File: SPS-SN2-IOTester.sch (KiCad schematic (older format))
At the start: 26 parts, among them J1 RJ45, J2 Spade Terminal, SW1 SW, SW2 SW, SW3 SW, SW4 SW, SW5 SW, SW6 SW, SW7 SW, SW8 SW

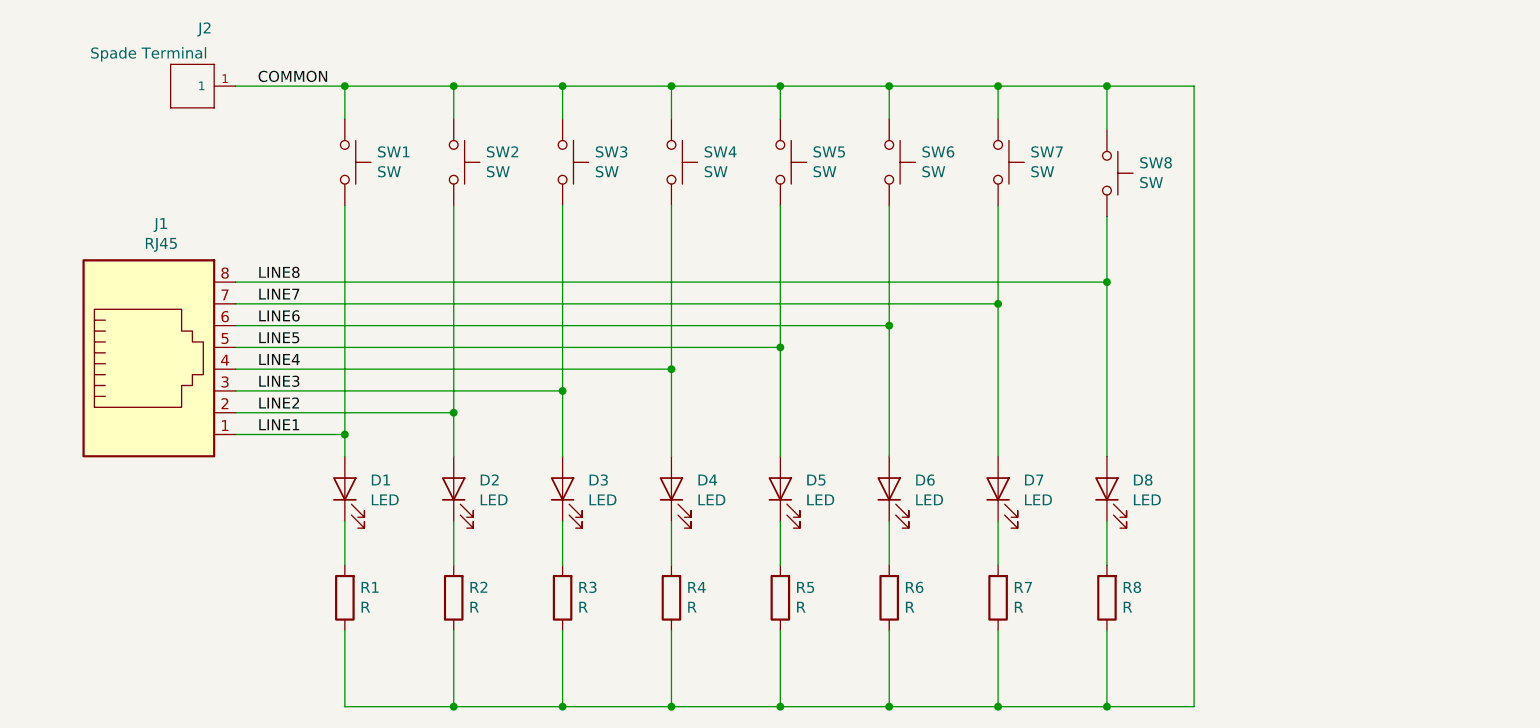
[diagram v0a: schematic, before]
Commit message: added schematic annotation
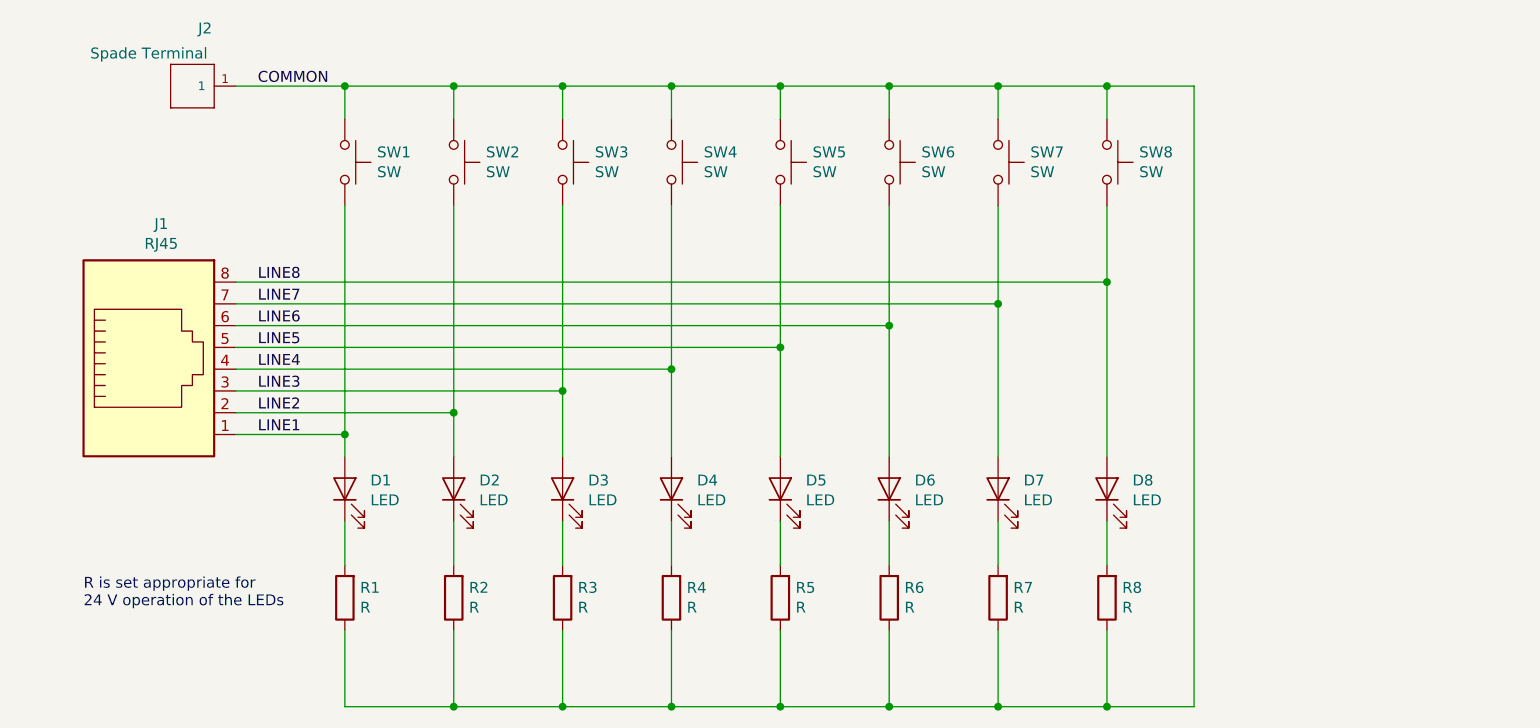
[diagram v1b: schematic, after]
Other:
- note added: "R is set appropriate for \n24 V operation of the LEDs"
- moved on the sheet: SW8
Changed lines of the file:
@@
 L Switch:SW_Push SW8
 U 1 1 5E0A6255
-P 7800 2600
-F 0 "SW8" V 7754 2748 50  0000 L CNN
-F 1 "SW" V 7845 2748 50  0000 L CNN
-F 2 "Button_Switch_THT:SW_PUSH_6mm_H5mm" H 7800 2800 50  0001 C CNN
-F 3 "~" H 7800 2800 50  0001 C CNN
-	1    7800 2600
+P 7800 2550
+F 0 "SW8" V 7754 2698 50  0000 L CNN
+F 1 "SW" V 7845 2698 50  0000 L CNN
+F 2 "Button_Switch_THT:SW_PUSH_6mm_H5mm" H 7800 2750 50  0001 C CNN
+F 3 "~" H 7800 2750 50  0001 C CNN
+	1    7800 2550
 	0    1    1    0
 $EndComp
-Wire Wire Line
-	7800 3100 7800 2800
 Connection ~ 7800 3100
 Wire Wire Line
@@
 	7300 2200 7300 2350
 Connection ~ 6800 2200
-Wire Wire Line
-	7300 2200 7800 2200
-Wire Wire Line
-	7800 2200 7800 2400
 Connection ~ 7300 2200
 Wire Wire Line
 	5800 5050 6300 5050
 Wire Wire Line
-	7800 2200 8200 2200
-Wire Wire Line
 	8200 2200 8200 5050
 Wire Wire Line
 	8200 5050 7800 5050
-Connection ~ 7800 2200
 Connection ~ 7800 5050
 $Comp
@@
 Text Label 3900 3100 0    50   ~ 0
 LINE8
+Wire Wire Line
+	7300 2200 7800 2200
+Wire Wire Line
+	7800 2350 7800 2200
+Connection ~ 7800 2200
+Wire Wire Line
+	7800 2200 8200 2200
+Wire Wire Line
+	7800 2750 7800 3100
+Text Notes 3100 4600 0    50   ~ 0
+R is set appropriate for \n24 V operation of the LEDs
 $EndSCHEMATC

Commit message: added DC barrel jack and moved resistors
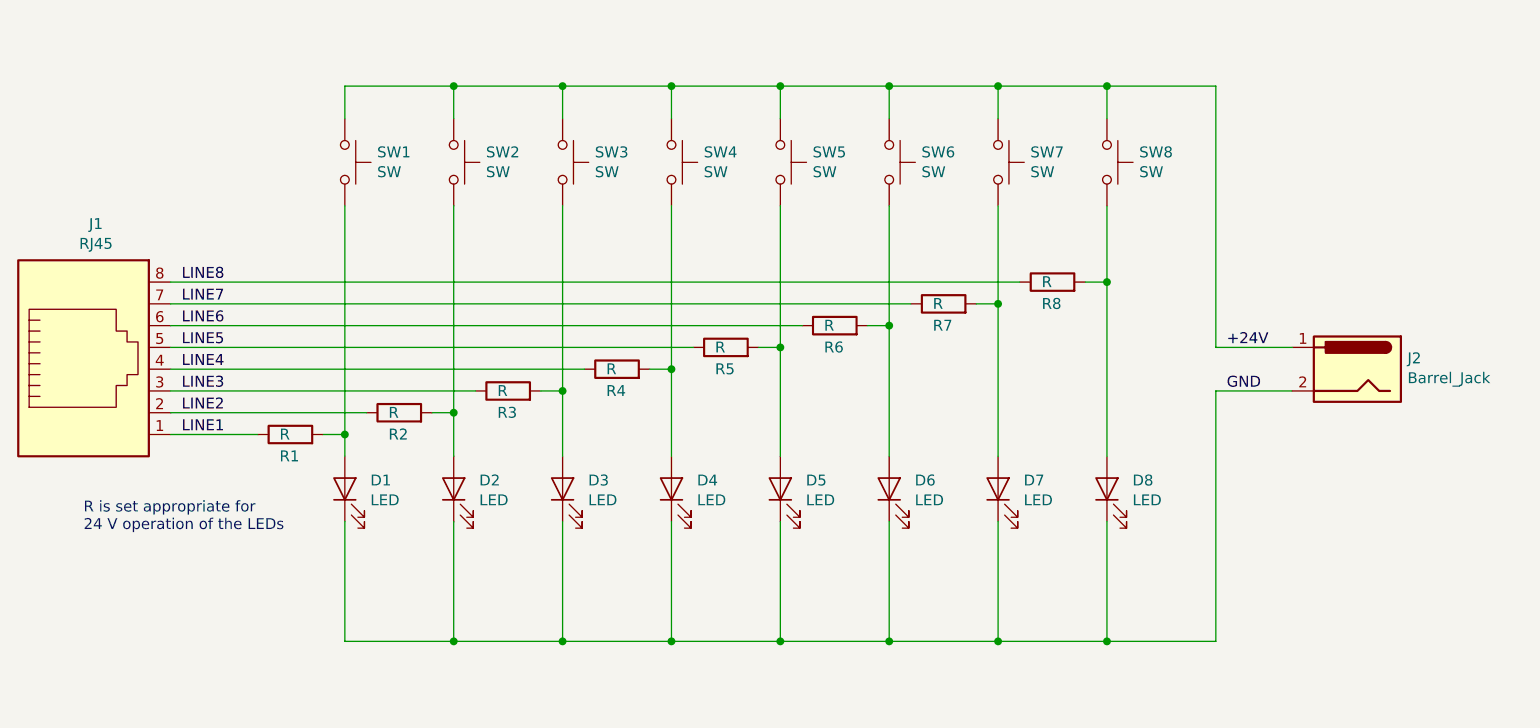
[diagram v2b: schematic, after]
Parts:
- removed J2: Spade Terminal, libs:TE_928814-1, symbol 928814-1:928814-1
- added J2: Barrel_Jack, Connector_BarrelJack:BarrelJack_Horizontal, symbol Connector:Barrel_Jack
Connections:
- net LINE1: now also R1.1; no longer D1.2 (A), SW1.2
- net LINE2: now also R2.1; no longer D2.2 (A), SW2.2
- net LINE3: now also R3.1; no longer D3.2 (A), SW3.2
- net LINE4: now also R4.1; no longer D4.2 (A), SW4.2
- net LINE5: now also R5.1; no longer D5.2 (A), SW5.2
- net LINE6: now also R6.1; no longer D6.2 (A), SW6.2
- net LINE7: now also R7.1; no longer D7.2 (A), SW7.2
- net LINE8: now also R8.1; no longer D8.2 (A), SW8.2
- net at R1.2: now also D1.2 (A), SW1.2; no longer D1.1 (K)
- net at R2.2: now also D2.2 (A), SW2.2; no longer D2.1 (K)
- net at R3.2: now also D3.2 (A), SW3.2; no longer D3.1 (K)
- net at R4.2: now also D4.2 (A), SW4.2; no longer D4.1 (K)
- net at R5.2: now also D5.2 (A), SW5.2; no longer D5.1 (K)
- net at R6.2: now also D6.2 (A), SW6.2; no longer D6.1 (K)
- net at R7.2: now also D7.2 (A), SW7.2; no longer D7.1 (K)
- net at R8.2: now also D8.2 (A), SW8.2; no longer D8.1 (K)
- net COMMON renamed +24V
- net +24V: now also J2.1; no longer R1.1, R2.1, R3.1, R4.1, R5.1, R6.1, R7.1, R8.1
- new net GND: D1.1 (K), D2.1 (K), D3.1 (K), D4.1 (K), D5.1 (K), D6.1 (K), D7.1 (K), D8.1 (K), J2.2
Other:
- moved on the sheet: J1, R1, R2, R3, R4, R5, R6, R7, R8

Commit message: swapped buttons and LEDs for enclosure versions
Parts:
- D1, D2, D3, D4, D5, D6, D7, D8: footprint LED_THT:LED_D3.0mm -> libs:LED_D3.0mm
- J2: footprint Connector_BarrelJack:BarrelJack_Horizontal -> SamacSys_Parts:BarrelJack_Horizontal
- SW1, SW2, SW3, SW4, SW5, SW6, SW7, SW8: footprint Button_Switch_THT:SW_PUSH_6mm_H5mm -> libs:SW_PUSH_6mm_H17mm
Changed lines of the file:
@@
 F 0 "D1" V 4339 3933 50  0000 R CNN
 F 1 "LED" V 4248 3933 50  0000 R CNN
-F 2 "LED_THT:LED_D3.0mm" H 4300 4050 50  0001 C CNN
+F 2 "libs:LED_D3.0mm" H 4300 4050 50  0001 C CNN
 F 3 "~" H 4300 4050 50  0001 C CNN
 	1    4300 4050
@@
 F 0 "D2" V 4839 3933 50  0000 R CNN
 F 1 "LED" V 4748 3933 50  0000 R CNN
-F 2 "LED_THT:LED_D3.0mm" H 4800 4050 50  0001 C CNN
+F 2 "libs:LED_D3.0mm" H 4800 4050 50  0001 C CNN
 F 3 "~" H 4800 4050 50  0001 C CNN
 	1    4800 4050
@@
 F 0 "D3" V 5339 3933 50  0000 R CNN
 F 1 "LED" V 5248 3933 50  0000 R CNN
-F 2 "LED_THT:LED_D3.0mm" H 5300 4050 50  0001 C CNN
+F 2 "libs:LED_D3.0mm" H 5300 4050 50  0001 C CNN
 F 3 "~" H 5300 4050 50  0001 C CNN
 	1    5300 4050
@@
 F 0 "D4" V 5839 3933 50  0000 R CNN
 F 1 "LED" V 5748 3933 50  0000 R CNN
-F 2 "LED_THT:LED_D3.0mm" H 5800 4050 50  0001 C CNN
+F 2 "libs:LED_D3.0mm" H 5800 4050 50  0001 C CNN
 F 3 "~" H 5800 4050 50  0001 C CNN
 	1    5800 4050
@@
 F 0 "D5" V 6339 3933 50  0000 R CNN
 F 1 "LED" V 6248 3933 50  0000 R CNN
-F 2 "LED_THT:LED_D3.0mm" H 6300 4050 50  0001 C CNN
+F 2 "libs:LED_D3.0mm" H 6300 4050 50  0001 C CNN
 F 3 "~" H 6300 4050 50  0001 C CNN
 	1    6300 4050
@@
 F 0 "D6" V 6839 3933 50  0000 R CNN
 F 1 "LED" V 6748 3933 50  0000 R CNN
-F 2 "LED_THT:LED_D3.0mm" H 6800 4050 50  0001 C CNN
+F 2 "libs:LED_D3.0mm" H 6800 4050 50  0001 C CNN
 F 3 "~" H 6800 4050 50  0001 C CNN
 	1    6800 4050
@@
 F 0 "D7" V 7339 3933 50  0000 R CNN
 F 1 "LED" V 7248 3933 50  0000 R CNN
-F 2 "LED_THT:LED_D3.0mm" H 7300 4050 50  0001 C CNN
+F 2 "libs:LED_D3.0mm" H 7300 4050 50  0001 C CNN
 F 3 "~" H 7300 4050 50  0001 C CNN
 	1    7300 4050
@@
 F 0 "D8" V 7839 3933 50  0000 R CNN
 F 1 "LED" V 7748 3933 50  0000 R CNN
-F 2 "LED_THT:LED_D3.0mm" H 7800 4050 50  0001 C CNN
+F 2 "libs:LED_D3.0mm" H 7800 4050 50  0001 C CNN
 F 3 "~" H 7800 4050 50  0001 C CNN
 	1    7800 4050
@@
 F 0 "SW1" V 4254 2698 50  0000 L CNN
 F 1 "SW" V 4345 2698 50  0000 L CNN
-F 2 "Button_Switch_THT:SW_PUSH_6mm_H5mm" H 4300 2750 50  0001 C CNN
+F 2 "libs:SW_PUSH_6mm_H17mm" H 4300 2750 50  0001 C CNN
 F 3 "~" H 4300 2750 50  0001 C CNN
 	1    4300 2550
@@
 F 0 "SW2" V 4754 2698 50  0000 L CNN
 F 1 "SW" V 4845 2698 50  0000 L CNN
-F 2 "Button_Switch_THT:SW_PUSH_6mm_H5mm" H 4800 2750 50  0001 C CNN
+F 2 "libs:SW_PUSH_6mm_H17mm" H 4800 2750 50  0001 C CNN
 F 3 "~" H 4800 2750 50  0001 C CNN
 	1    4800 2550
@@
 F 0 "SW3" V 5254 2698 50  0000 L CNN
 F 1 "SW" V 5345 2698 50  0000 L CNN
-F 2 "Button_Switch_THT:SW_PUSH_6mm_H5mm" H 5300 2750 50  0001 C CNN
+F 2 "libs:SW_PUSH_6mm_H17mm" H 5300 2750 50  0001 C CNN
 F 3 "~" H 5300 2750 50  0001 C CNN
 	1    5300 2550
@@
 F 0 "SW4" V 5754 2698 50  0000 L CNN
 F 1 "SW" V 5845 2698 50  0000 L CNN
-F 2 "Button_Switch_THT:SW_PUSH_6mm_H5mm" H 5800 2750 50  0001 C CNN
+F 2 "libs:SW_PUSH_6mm_H17mm" H 5800 2750 50  0001 C CNN
 F 3 "~" H 5800 2750 50  0001 C CNN
 	1    5800 2550
@@
 F 0 "SW5" V 6254 2698 50  0000 L CNN
 F 1 "SW" V 6345 2698 50  0000 L CNN
-F 2 "Button_Switch_THT:SW_PUSH_6mm_H5mm" H 6300 2750 50  0001 C CNN
+F 2 "libs:SW_PUSH_6mm_H17mm" H 6300 2750 50  0001 C CNN
 F 3 "~" H 6300 2750 50  0001 C CNN
 	1    6300 2550
@@
 F 0 "SW6" V 6754 2698 50  0000 L CNN
 F 1 "SW" V 6845 2698 50  0000 L CNN
-F 2 "Button_Switch_THT:SW_PUSH_6mm_H5mm" H 6800 2750 50  0001 C CNN
+F 2 "libs:SW_PUSH_6mm_H17mm" H 6800 2750 50  0001 C CNN
 F 3 "~" H 6800 2750 50  0001 C CNN
 	1    6800 2550
@@
 F 0 "SW7" V 7254 2698 50  0000 L CNN
 F 1 "SW" V 7345 2698 50  0000 L CNN
-F 2 "Button_Switch_THT:SW_PUSH_6mm_H5mm" H 7300 2750 50  0001 C CNN
+F 2 "libs:SW_PUSH_6mm_H17mm" H 7300 2750 50  0001 C CNN
 F 3 "~" H 7300 2750 50  0001 C CNN
 	1    7300 2550
@@
 F 0 "SW8" V 7754 2698 50  0000 L CNN
 F 1 "SW" V 7845 2698 50  0000 L CNN
-F 2 "Button_Switch_THT:SW_PUSH_6mm_H5mm" H 7800 2750 50  0001 C CNN
+F 2 "libs:SW_PUSH_6mm_H17mm" H 7800 2750 50  0001 C CNN
 F 3 "~" H 7800 2750 50  0001 C CNN
 	1    7800 2550
@@
 F 0 "J2" H 8720 3550 50  0000 R CNN
 F 1 "Barrel_Jack" H 8720 3459 50  0000 R CNN
-F 2 "Connector_BarrelJack:BarrelJack_Horizontal" H 9000 3460 50  0001 C CNN
+F 2 "SamacSys_Parts:BarrelJack_Horizontal" H 9000 3460 50  0001 C CNN
 F 3 "~" H 9000 3460 50  0001 C CNN
 	1    8950 3500

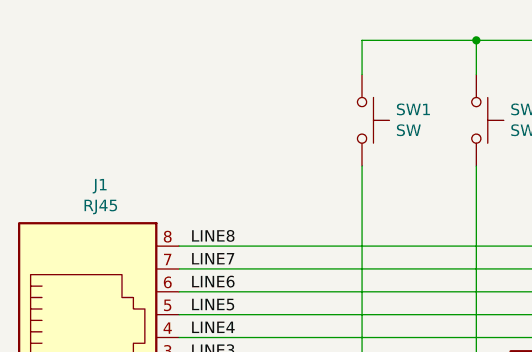
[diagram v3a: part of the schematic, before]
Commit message: Latest version with mounting holes
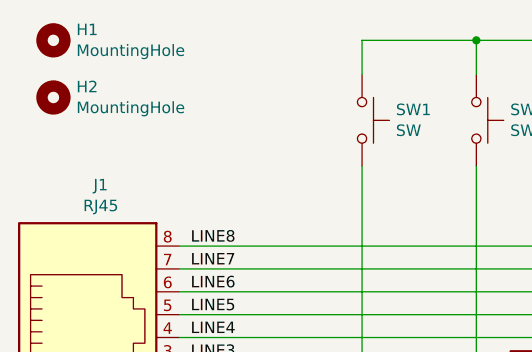
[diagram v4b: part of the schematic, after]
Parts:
- added H1, H2: MountingHole, MountingHole:MountingHole_2.2mm_M2, symbol Mechanical:MountingHole
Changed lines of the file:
@@
 Wire Wire Line
 	8300 4750 8300 3600
+$Comp
+L Mechanical:MountingHole H1
+U 1 1 5E112557
+P 2950 2200
+F 0 "H1" H 3050 2246 50  0000 L CNN
+F 1 "MountingHole" H 3050 2155 50  0000 L CNN
+F 2 "MountingHole:MountingHole_2.2mm_M2" H 2950 2200 50  0001 C CNN
+F 3 "~" H 2950 2200 50  0001 C CNN
+	1    2950 2200
+	1    0    0    -1
+$EndComp
+$Comp
+L Mechanical:MountingHole H2
+U 1 1 5E112A40
+P 2950 2450
+F 0 "H2" H 3050 2496 50  0000 L CNN
+F 1 "MountingHole" H 3050 2405 50  0000 L CNN
+F 2 "MountingHole:MountingHole_2.2mm_M2" H 2950 2450 50  0001 C CNN
+F 3 "~" H 2950 2450 50  0001 C CNN
+	1    2950 2450
+	1    0    0    -1
+$EndComp
 $EndSCHEMATC

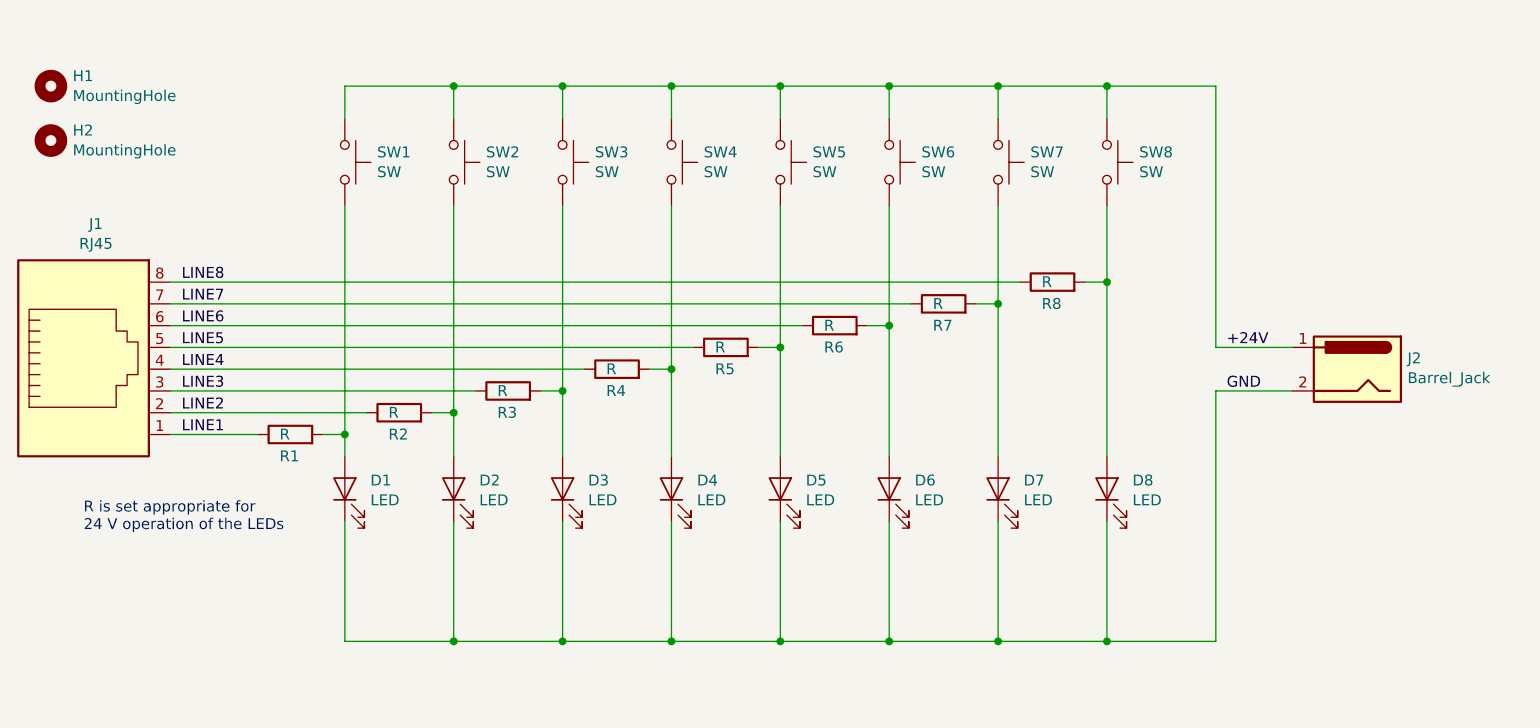
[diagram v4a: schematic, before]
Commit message: Redesigned circuit to prevent switches blowing LEDs
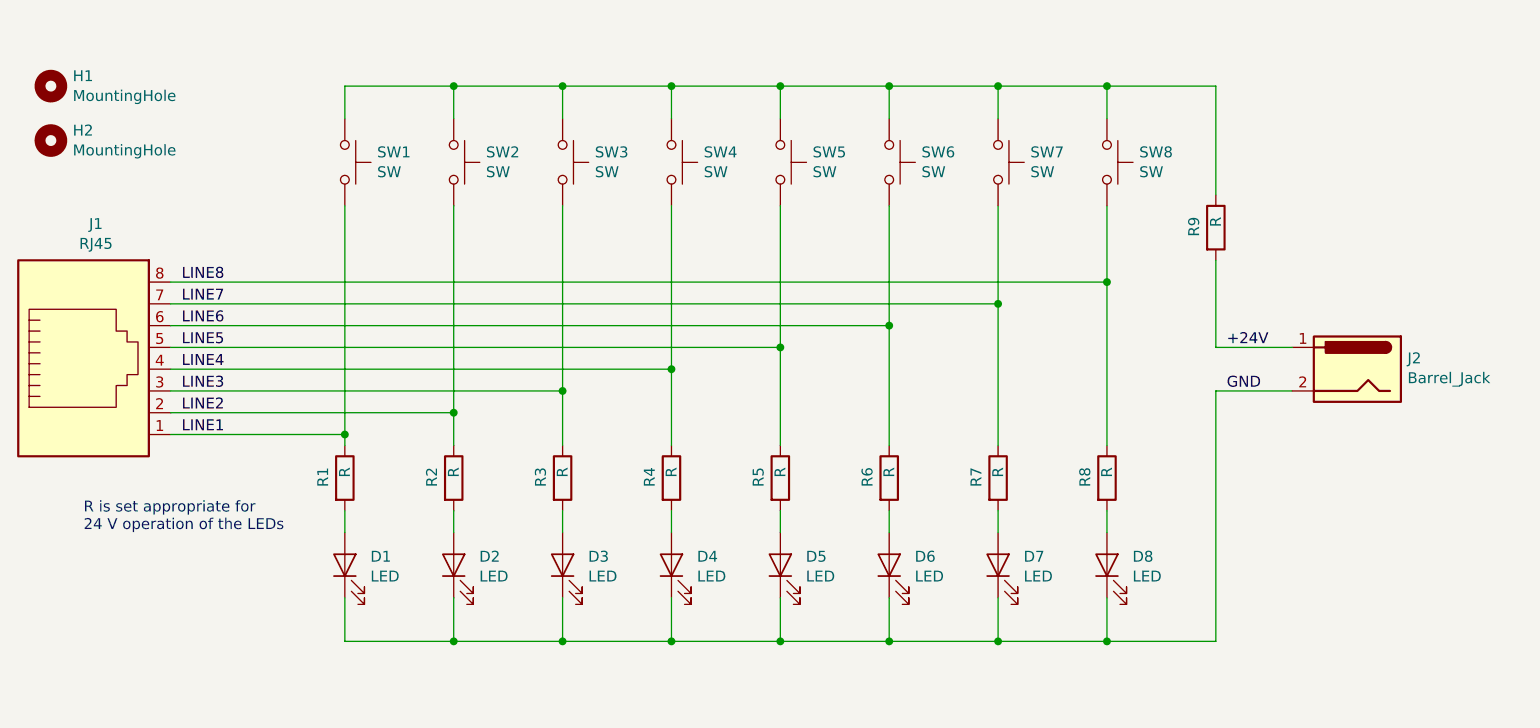
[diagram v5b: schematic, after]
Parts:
- added R9: R, Resistor_THT:R_Axial_DIN0207_L6.3mm_D2.5mm_P7.62mm_Horizontal, symbol Device:R
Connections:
- net +24V: now also R9.2; no longer SW1.1, SW2.1, SW3.1, SW4.1, SW5.1, SW6.1, SW7.1, SW8.1
- net LINE1: now also SW1.2
- net LINE2: now also SW2.2
- net LINE3: now also SW3.2
- net LINE4: now also SW4.2
- net LINE5: now also SW5.2
- net LINE6: now also SW6.2
- net LINE7: now also SW7.2
- net LINE8: now also SW8.2
- net at D1.2 (A), R1.2: no longer SW1.2
- net at D2.2 (A), R2.2: no longer SW2.2
- net at D3.2 (A), R3.2: no longer SW3.2
- net at D4.2 (A), R4.2: no longer SW4.2
- net at D5.2 (A), R5.2: no longer SW5.2
- net at D6.2 (A), R6.2: no longer SW6.2
- net at D7.2 (A), R7.2: no longer SW7.2
- net at D8.2 (A), R8.2: no longer SW8.2
- new net: R9.1, SW1.1, SW2.1, SW3.1, SW4.1, SW5.1, SW6.1, SW7.1, SW8.1
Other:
- moved on the sheet: D1, D2, D3, D4, D5, D6, D7, D8, R1, R2, R3, R4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
